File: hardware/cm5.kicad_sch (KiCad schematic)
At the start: 4 parts, among them J7 Conn_02x07_Odd_Even

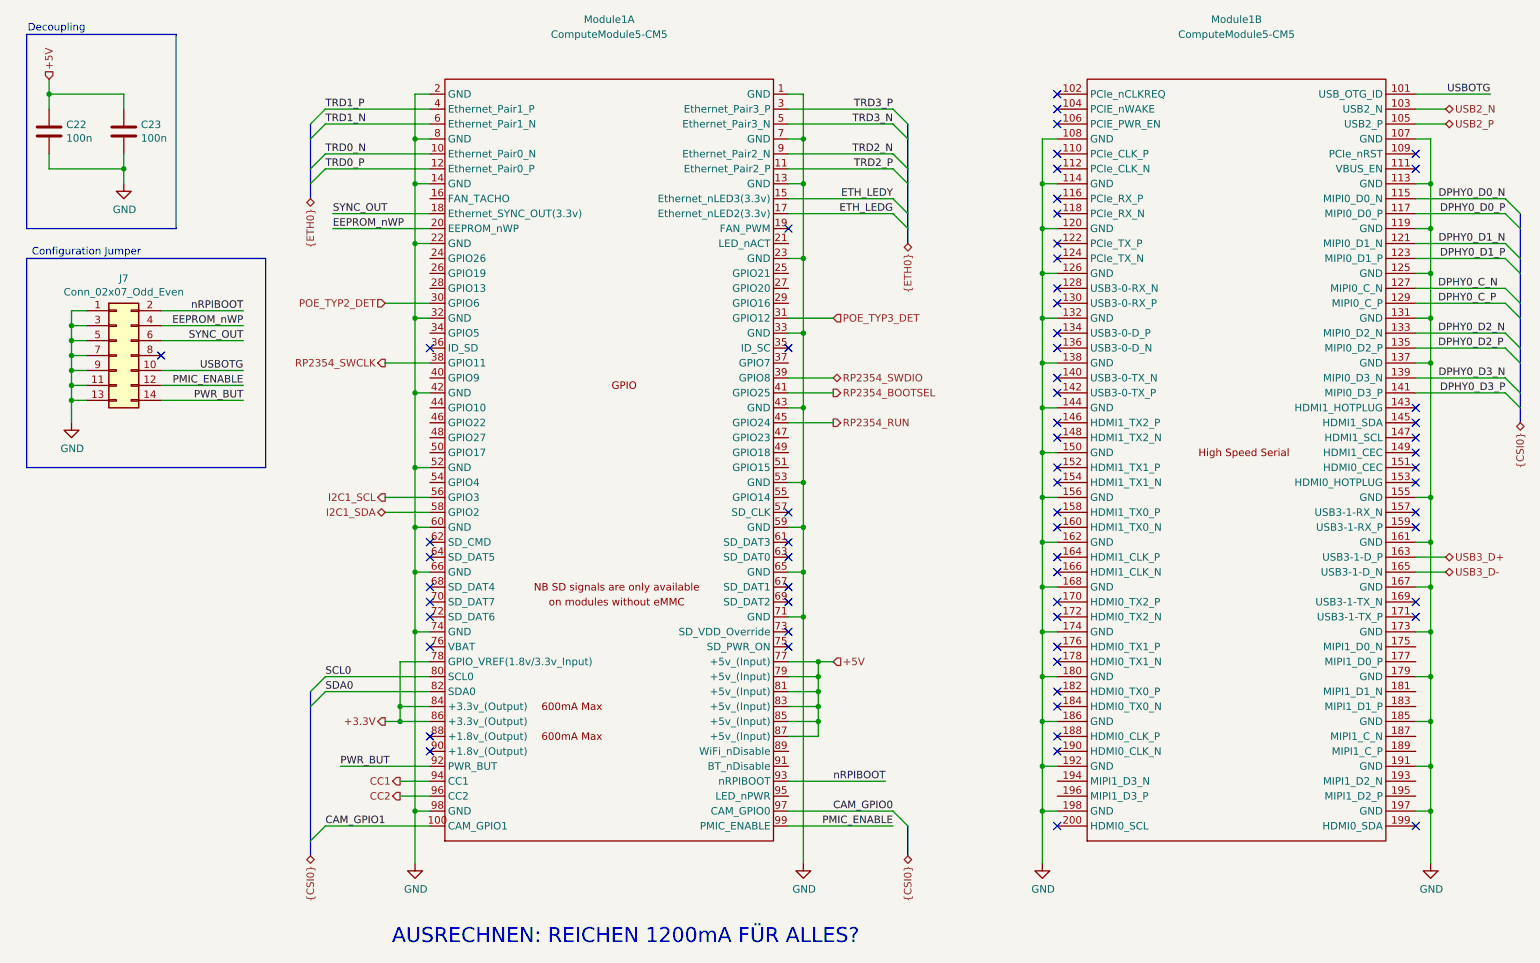
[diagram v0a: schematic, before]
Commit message: Add second camera, magnet load switch and schematic fixes
- Second camera J11 on MIPI1: I2C on ID_SD/ID_SC with 2.2k pull-ups,
  power enable on GPIO14/15 (CAM1_GPIO0/1); both cameras take 3.3 V
  from CM5_3.3V
- Magnet power switch: IC9 output is now +5V_AON, TPS22965 load switch
  IC15 drives +5V, J12 carries +5V_AON / MAG_ON / GND with R29
  pull-down; new TPS22965 symbol library
- Power: 4 A TPSM53604, 8 mOhm input sense resistor, C39/C40 bulk caps,
  F1-F3 battery polyfuses; 5 V raised to 5.115 V (R24 2.43k, 0.5 %
  feedback resistors); 47 uF at the CM5 5 V pins
- BMI270 on SPI and WSEN-PADS on I2C in serial_peripherals.kicad_sch
- Breakout headers J9/J13 with 5 V, 3.3 V and GND
- References renamed U -> IC; net classes for DPHY1, +5V, +5V_AON, +3.3V
- ERC clean (0 errors, 0 warnings); PCB update from the schematic is
  still in progress

Co-Authored-By: Claude Opus 5.5 <noreply@anthropic.com>
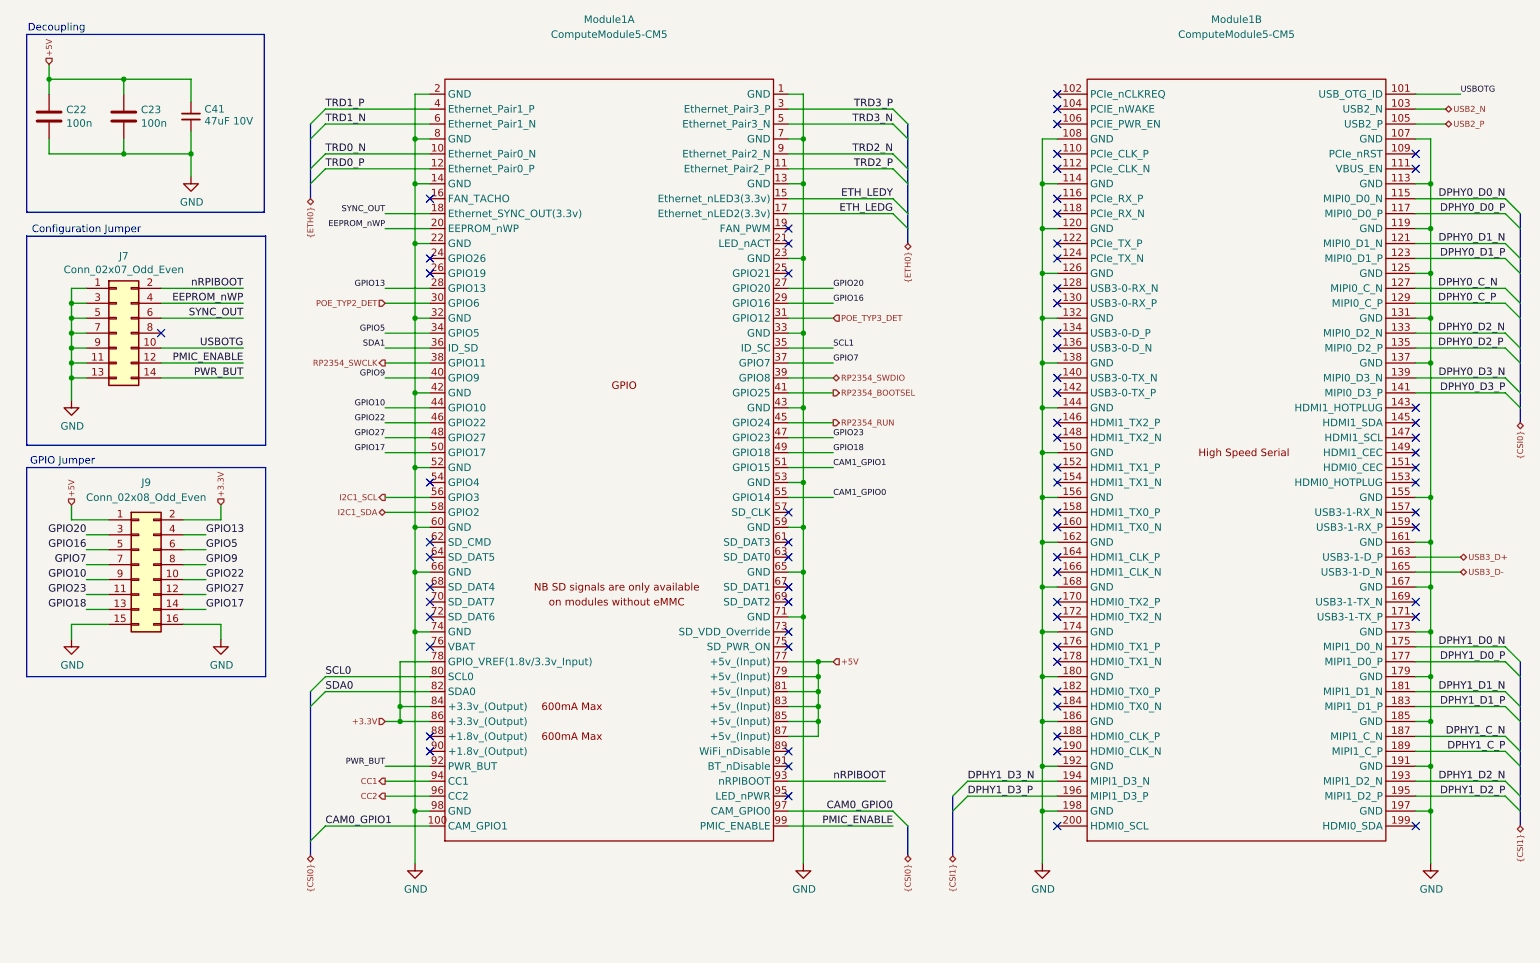
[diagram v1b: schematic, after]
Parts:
- added C41: 47uF 10V, Capacitor_SMD:C_1210_3225Metric, symbol Device:C_Small
- added J9: Conn_02x08_Odd_Even, Connector_PinHeader_1.27mm:PinHeader_2x08_P1.27mm_Vertical, symbol Connector_Generic:Conn_02x08_Odd_Even
- J7: footprint Connector_PinHeader_2.54mm:PinHeader_2x07_P2.54mm_Vertical -> Connector_PinHeader_1.27mm:PinHeader_2x07_P1.27mm_Vertical
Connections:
- net +3.3V: now also J9.2 (Pin_2)
- net +5V: now also C41.1, J9.1 (Pin_1)
- net GND: now also C41.2, J9.15 (Pin_15), J9.16 (Pin_16)
- net DPHY1_D0_N: now reaches Module1.175 (MIPI1_D0_N)
- net DPHY1_D0_P: now reaches Module1.177 (MIPI1_D0_P)
- net DPHY1_D1_N: now reaches Module1.181 (MIPI1_D1_N)
- net DPHY1_D1_P: now reaches Module1.183 (MIPI1_D1_P)
- net DPHY1_C_N: now reaches Module1.187 (MIPI1_C_N)
- net DPHY1_C_P: now reaches Module1.189 (MIPI1_C_P)
- net DPHY1_D2_N: now reaches Module1.193 (MIPI1_D2_N)
- net DPHY1_D3_N: now reaches Module1.194 (MIPI1_D3_N)
- net DPHY1_D2_P: now reaches Module1.195 (MIPI1_D2_P)
- net DPHY1_D3_P: now reaches Module1.196 (MIPI1_D3_P)
- net GPIO20: now reaches Module1.27 (GPIO20)
- net GPIO20: now also J9.3 (Pin_3)
- net GPIO13: now reaches Module1.28 (GPIO13)
- net GPIO13: now also J9.4 (Pin_4)
- net GPIO16: now reaches Module1.29 (GPIO16)
- net GPIO16: now also J9.5 (Pin_5)
- net GPIO5: now reaches Module1.34 (GPIO5)
- net GPIO5: now also J9.6 (Pin_6)
- net SCL1: now reaches Module1.35 (ID_SC)
- net SDA1: now reaches Module1.36 (ID_SD)
- net GPIO7: now reaches Module1.37 (GPIO7)
- net GPIO7: now also J9.7 (Pin_7)
- net GPIO9: now reaches Module1.40 (GPIO9)
- net GPIO9: now also J9.8 (Pin_8)
- net GPIO10: now reaches Module1.44 (GPIO10)
- net GPIO10: now also J9.9 (Pin_9)
- net GPIO22: now reaches Module1.46 (GPIO22)
- net GPIO22: now also J9.10 (Pin_10)
- net GPIO23: now reaches Module1.47 (GPIO23)
- net GPIO23: now also J9.11 (Pin_11)
- net GPIO27: now reaches Module1.48 (GPIO27)
- net GPIO27: now also J9.12 (Pin_12)
- net GPIO18: now reaches Module1.49 (GPIO18)
- net GPIO18: now also J9.13 (Pin_13)
- net GPIO17: now reaches Module1.50 (GPIO17)
- net GPIO17: now also J9.14 (Pin_14)
- net CAM1_GPIO1: now reaches Module1.51 (GPIO15)
- net CAM1_GPIO0: now reaches Module1.55 (GPIO14)
- net CAM_GPIO0 renamed CAM0_GPIO0
- net CAM_GPIO1 renamed CAM0_GPIO1
- no-connect marks 64 -> 71
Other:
- note added: "GPIO Jumper"
- note removed: "AUSRECHNEN: REICHEN 1200mA FÜR ALLES?"
- moved on the sheet: C22, C23, J7

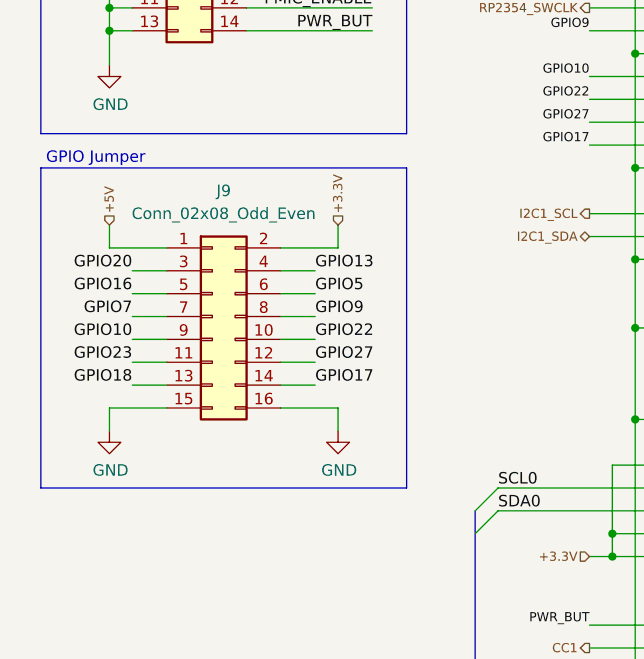
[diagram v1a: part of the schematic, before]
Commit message: Separate the supply pins on breakout headers J9 and J13
Both headers now start with +5V, GND, GND, +3.3V (pins 1-4), so 5 V
and 3.3 V only meet diagonally and each supply pin has GND beside it.
The GPIOs that sat on pins 3/4 moved to the end of each header.

Co-Authored-By: Claude Opus 5.5 <noreply@anthropic.com>
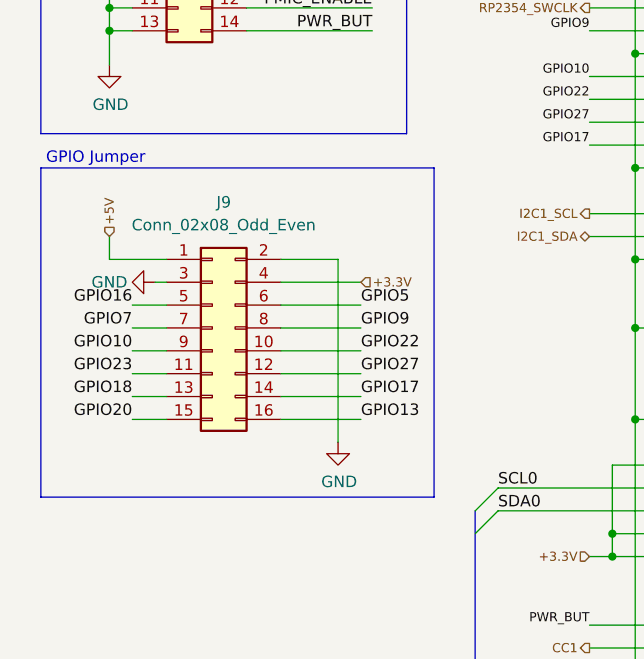
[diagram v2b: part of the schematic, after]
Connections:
- net +3.3V: now also J9.4 (Pin_4); no longer J9.2 (Pin_2)
- net GND: now also J9.2 (Pin_2), J9.3 (Pin_3); no longer J9.15 (Pin_15), J9.16 (Pin_16)
- net GPIO13: now also J9.16 (Pin_16); no longer J9.4 (Pin_4)
- net GPIO20: now also J9.15 (Pin_15); no longer J9.3 (Pin_3)
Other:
- moved on the sheet: J9

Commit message: Redo the PCB layout: 70 x 90 mm, power section grouped, one-side reflow
- Second camera connector J11 beside J5 on the top edge.
- SHT45 on a slotted tongue (no pour, no vias, four tracks over a 2.5 mm
  bridge) for thermal decoupling.
- All fine-pitch parts on top; the bottom holds only hand-solderable parts
  (IC5, connectors, 0603+ passives, fuses, electrolytics).
- MagJack, PoE module, charger, 5 V buck and battery connector grouped in
  the bottom half.
- Four M2 mounting holes H1-H4; silkscreen labels for the connectors and
  pin tables for J7, J9 and J13 on the bottom.
- Header pins remapped to simplify routing: J9 (CM5 GPIO), J13 (RP2354A
  GPIO22-29) and J7 (CM5 config); schematic labels updated to match.
- Default clearance 0.1 mm; DRC rules for C20's thermal, top parts under the
  CM5, IC10's land pattern and the edge parts.
- DRC: 0 errors, schematic parity clean; one expected unconnected item
  (CM5 connector-A GND pin 7, tied inside the CM5).

Co-Authored-By: Claude Opus 5.5 <noreply@anthropic.com>
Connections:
- net EEPROM_nWP: now also J7.12 (Pin_12); no longer J7.4 (Pin_4)
- net GPIO10: now also J9.7 (Pin_7); no longer J9.9 (Pin_9)
- net GPIO13: now also J9.6 (Pin_6); no longer J9.16 (Pin_16)
- net GPIO16: now also J9.15 (Pin_15); no longer J9.5 (Pin_5)
- net GPIO17: now also J9.8 (Pin_8); no longer J9.14 (Pin_14)
- net GPIO18: now also J9.11 (Pin_11); no longer J9.13 (Pin_13)
- net GPIO20: now also J9.16 (Pin_16); no longer J9.15 (Pin_15)
- net GPIO23: now also J9.14 (Pin_14); no longer J9.11 (Pin_11)
- net GPIO27: now also J9.9 (Pin_9); no longer J9.12 (Pin_12)
- net GPIO5: now also J9.12 (Pin_12); no longer J9.6 (Pin_6)
- net GPIO7: now also J9.13 (Pin_13); no longer J9.7 (Pin_7)
- net GPIO9: now also J9.5 (Pin_5); no longer J9.8 (Pin_8)
- net PMIC_ENABLE: now also J7.6 (Pin_6); no longer J7.12 (Pin_12)
- net PWR_BUT: now also J7.4 (Pin_4); no longer J7.14 (Pin_14)
- net SYNC_OUT: now also J7.14 (Pin_14); no longer J7.6 (Pin_6)
- net USBOTG: now also J7.2 (Pin_2); no longer J7.10 (Pin_10)
- net nRPIBOOT: now also J7.10 (Pin_10); no longer J7.2 (Pin_2)
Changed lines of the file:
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@@
 	(wire
 		(pts
+			(xy 48.26 101.6) (xy 48.26 121.92)
+		)
+		(stroke
+			(width 0)
+			(type default)
+		)
+	)
+	(wire
+		(pts
 			(xy 76.2 48.26) (xy 83.82 48.26)
 		)
@@
 	(wire
 		(pts
+			(xy 50.8 99.06) (xy 50.8 104.14)
+		)
+		(stroke
+			(width 0)
+			(type default)
+		)
+	)
+	(wire
+		(pts
 			(xy 76.2 50.8) (xy 83.82 50.8)
 		)
@@
 	(wire
 		(pts
+			(xy 26.67 121.92) (xy 26.67 104.14)
+		)
+		(stroke
+			(width 0)
+			(type default)
+		)
+	)
+	(wire
+		(pts
 			(xy 254 134.62) (xy 254 127)
 		)
@@
 	(wire
 		(pts
+			(xy 41.91 104.14) (xy 50.8 104.14)
+		)
+		(stroke
+			(width 0)
+			(type default)
+		)
+	)
+	(wire
+		(pts
 			(xy 144.78 38.1) (xy 162.56 38.1)
 		)
@@
 	(wire
 		(pts
+			(xy 26.67 104.14) (xy 29.21 104.14)
+		)
+		(stroke
+			(width 0)
+			(type default)
+		)
+	)
+	(wire
+		(pts
 			(xy 144.78 33.02) (xy 162.56 33.02)
 		)
@@
 		)
 	)
-	(label "GPIO27"
+	(label "GPIO5"
 		(at 50.8 114.3 0)
 		(effects
@@
 		)
 	)
-	(label "GPIO9"
+	(label "GPIO17"
 		(at 50.8 109.22 0)
 		(effects
@@
 		)
 	)
-	(label "EEPROM_nWP"
+	(label "PWR_BUT"
 		(at 52.07 63.5 180)
 		(effects
@@
 		)
 	)
-	(label "GPIO16"
+	(label "GPIO9"
 		(at 25.4 106.68 180)
 		(effects
@@
 		)
 	)
-	(label "SYNC_OUT"
+	(label "PMIC_ENABLE"
 		(at 52.07 66.04 180)
 		(effects
@@
 		)
 	)
-	(label "GPIO7"
+	(label "GPIO10"
 		(at 25.4 109.22 180)
 		(effects
@@
 		)
 	)
-	(label "GPIO13"
+	(label "GPIO20"
 		(at 50.8 119.38 0)
 		(effects
@@
 		)
 	)
-	(label "PMIC_ENABLE"
+	(label "EEPROM_nWP"
 		(at 52.07 73.66 180)
 		(effects
@@
 		)
 	)
-	(label "GPIO10"
+	(label "GPIO27"
 		(at 25.4 111.76 180)
 		(effects
@@
 		)
 	)
-	(label "USBOTG"
+	(label "nRPIBOOT"
 		(at 52.07 71.12 180)
 		(effects
@@
 		)
 	)
-	(label "GPIO20"
+	(label "GPIO16"
 		(at 25.4 119.38 180)
 		(effects
@@
 		)
 	)
-	(label "nRPIBOOT"
+	(label "USBOTG"
 		(at 52.07 60.96 180)
 		(effects
@@
 		)
 	)
-	(label "GPIO17"
+	(label "GPIO23"
 		(at 50.8 116.84 0)
 		(effects
@@
 		)
 	)
-	(label "GPIO18"
+	(label "GPIO7"
 		(at 25.4 116.84 180)
 		(effects
@@
 		)
 	)
-	(label "GPIO5"
+	(label "GPIO13"
 		(at 50.8 106.68 0)
 		(effects
@@
 		)
 	)
-	(label "GPIO23"
+	(label "GPIO18"
 		(at 25.4 114.3 180)
 		(effects
@@
 		)
 	)
-	(label "PWR_BUT"
+	(label "SYNC_OUT"
 		(at 52.07 76.2 180)
 		(effects
@@
 		)
 	)
+	(hierarchical_label "+3.3V"
+		(shape input)
+		(at 50.8 99.06 90)
+		(effects
+			(font
+				(size 1.016 1.016)
+			)
+			(justify left)
+		)
+	)
 	(hierarchical_label "USB3_D+"
 		(shape bidirectional)
@@
 	(symbol
 		(lib_id "power:GND")
+		(at 26.67 121.92 0)
+		(unit 1)
+		(body_style 1)
+		(exclude_from_sim no)
+		(in_bom yes)
+		(on_board yes)
+		(in_pos_files yes)
+		(dnp no)
+		(property "Reference" "#PWR0172"
+			(at 26.67 128.27 0)
+			(hide yes)
+			(show_name no)
+			(do_not_autoplace no)
+			(effects
+				(font
+					(size 1.27 1.27)
+				)
+			)
+		)
+		(property "Value" "GND"
+			(at 26.797 126.3142 0)
+			(show_name no)
+			(do_not_autoplace no)
+			(effects
+				(font
+					(size 1.27 1.27)
+				)
+			)
+		)
+		(property "Footprint" ""
+			(at 26.67 121.92 0)
+			(hide yes)
+			(show_name no)
+			(do_not_autoplace no)
+			(effects
+				(font
+					(size 1.27 1.27)
+				)
+			)
+		)
+		(property "Datasheet" ""
+			(at 26.67 121.92 0)
+			(hide yes)
+			(show_name no)
+			(do_not_autoplace no)
+			(effects
+				(font
+					(size 1.27 1.27)
+				)
+			)
+		)
+		(property "Description" "Power symbol creates a global label with name \"GND\" , ground"
+			(at 26.67 121.92 0)
+			(hide yes)
+			(show_name no)
+			(do_not_autoplace no)
+			(effects
+				(font
+					(size 1.27 1.27)
+				)
+			)
+		)
+		(pin "1"
+		)
+		(instances
+			(project "manafish"
+				(path "/37283e3e-a087-4659-9b29-171eab26a1f6/66118e41-f515-4bf7-aa29-701c06daff5b"
+					(reference "#PWR0172")
+					(unit 1)
+				)
+			)
+		)
+	)
+	(symbol
+		(lib_id "power:GND")
 		(at 22.86 80.01 0)
 		(unit 1)
@@
 					(unit 1)
 				)
-			)
-		)
-	)
-	(wire
-		(pts
-			(xy 48.26 101.6) (xy 48.26 121.92)
-		)
-		(stroke
-			(width 0)
-			(type default)
-		)
-	)
-	(wire
-		(pts
-			(xy 41.91 104.14) (xy 50.8 104.14)
-		)
-		(stroke
-			(width 0)
-			(type default)
-		)
-	)
-	(hierarchical_label "+3.3V"
-		(shape input)
-		(at 50.8 104.14 0)
-		(effects
-			(font
-				(size 1.016 1.016)
-			)
-			(justify left)
-		)
-	)
-	(wire
-		(pts
-			(xy 29.21 104.14) (xy 27.94 104.14)
-		)
-		(stroke
-			(width 0)
-			(type default)
-		)
-	)
-	(symbol
-		(lib_id "power:GND")
-		(at 27.94 104.14 270)
-		(unit 1)
-		(body_style 1)
-		(exclude_from_sim no)
-		(in_bom no)
-		(on_board no)
-		(in_pos_files no)
-		(dnp no)
-		(property "Reference" "#PWR0176"
-			(at 21.59 104.14 90)
-			(hide yes)
-			(show_name no)
-			(do_not_autoplace no)
-			(effects
-				(font
-					(size 1.27 1.27)
-				)
-			)
-		)
-		(property "Value" "GND"
-			(at 22.86 104.14 90)
-			(show_name no)
-			(do_not_autoplace no)
-			(effects
-				(font
-					(size 1.27 1.27)
-				)
-			)
-		)
-		(property "Footprint" ""
-			(at 27.94 104.14 0)
-			(hide yes)
-			(show_name no)
-			(do_not_autoplace no)
-			(effects
-				(font
-					(size 1.27 1.27)
-				)
-			)
-		)
-		(property "Datasheet" ""
-			(at 27.94 104.14 0)
-			(hide yes)
-			(show_name no)
-			(do_not_autoplace no)
-			(effects
-				(font
-					(size 1.27 1.27)
-				)
-			)
-		)
-		(property "Description" "Power symbol creates a global label with name \"GND\" , ground"
-			(at 27.94 104.14 0)
-			(hide yes)
-			(show_name no)
-			(do_not_autoplace no)
-			(effects
-				(font
-					(size 1.27 1.27)
-				)
-			)
-		)
-		(pin "1"
-		)
-		(instances
-			(project "manafish"
-				(path "/37283e3e-a087-4659-9b29-171eab26a1f6/66118e41-f515-4bf7-aa29-701c06daff5b"
-					(reference "#PWR0176")
-					(unit 1)
-				)
